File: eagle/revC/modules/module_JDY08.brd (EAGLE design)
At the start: 24.1 x 32.8 mm, 32 parts

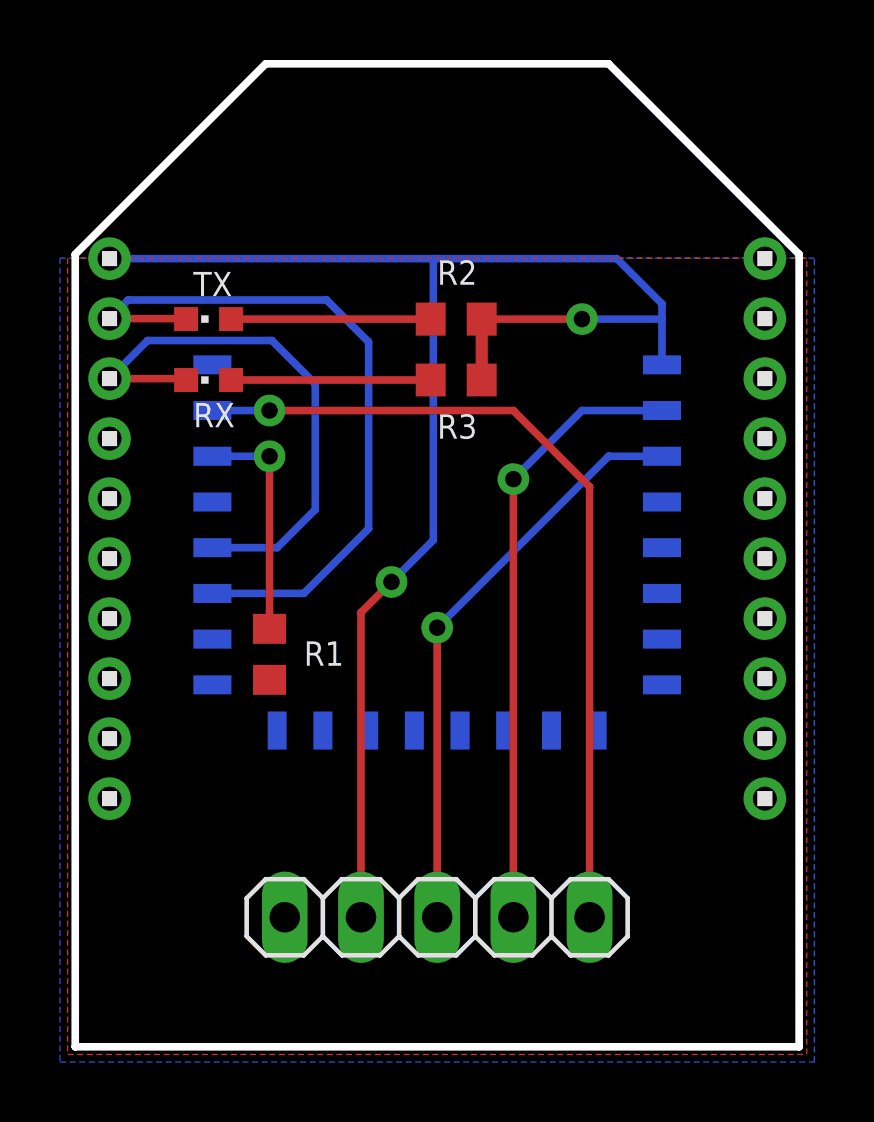
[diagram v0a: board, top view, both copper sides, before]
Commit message: Replaced modules with library parts
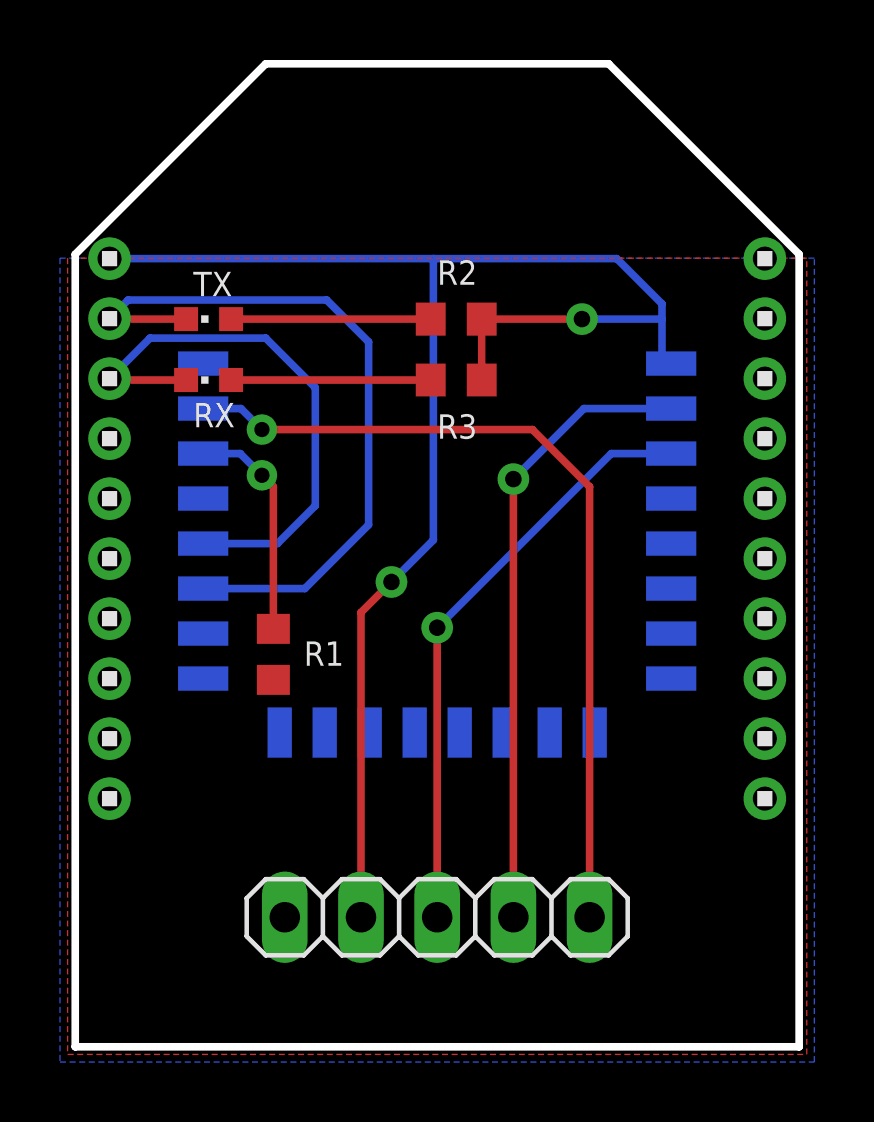
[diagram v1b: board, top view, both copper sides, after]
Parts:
- removed GND, P00, P01, P02, P03, P04, P05, P06, P07, P10, P11, P12, P13, P14, P15, P16, P17, P20, P21, P22, RST, SCL, SDA, VCC: (no value), wirepad:SMD0,65-1,27
- added U$1: JDY08, RadioShield:JDY08
- moved R1 0.13 mm to (6.73, 13.2), turned to 270 degrees
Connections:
- removed net N$5: LEFT1.3, P02.1, RX.C
- removed net N$6: LEFT1.2, P03.1, TX.C
- new net N$10: R1.1, U$1.P00
- new net N$11: LEFT1.2, TX.C, U$1.TXD
- net GND: now also R1.2, U$1.GND; no longer GND.1, R1.1
- net N$1: now also U$1.RST; no longer RST.1
- net N$2: now also U$1.P21; no longer P21.1
- net N$3: now also U$1.P22; no longer P22.1
- net N$4: now also LEFT1.3, RX.C, U$1.RXD; no longer P00.1, R1.2
- net VCC: now also U$1.VCC; no longer VCC.1
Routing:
- net N$11: track 0.00 -> 24.5 mm
- net N$6: track 24.4 -> 0.00 mm
- net N$5: track 18.7 -> 0.00 mm
- net N$4: track 7.66 -> 18.9 mm, vias 1 -> 0
- net N$10: track 0.00 -> 7.53 mm, vias 0 -> 1
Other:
- board text removed: "P00"
- board text removed: "P01"
- board text removed: "P02"
- board text removed: "P03"
- board text removed: "P04"
- board text removed: "P05"
- board text removed: "P06"
- board text removed: "P07"
- board text removed: "P10"
- board text removed: "P11"
- board text removed: "P12"
- board text removed: "P13"
- board text removed: "P14"
- board text removed: "P15"
- board text removed: "P16"
- board text removed: "P17"
- board text removed: "P20"
- board text removed: "P21"
- board text removed: "P22"
- board text removed: "SCL"
- board text removed: "SDA"

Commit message: Fixed module name layers
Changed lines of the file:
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@@
 <wire x1="24.257" y1="26.543" x2="24.257" y2="0.127" width="0.254" layer="20"/>
 <wire x1="24.257" y1="0.127" x2="0.127" y2="0.127" width="0.254" layer="20"/>
-<text x="16.383" y="1.778" size="0.8128" layer="51" font="vector" ratio="15" rot="SR0">RST</text>
-<text x="11.303" y="1.778" size="0.8128" layer="51" font="vector" ratio="15" rot="SR0">DAT</text>
-<text x="13.843" y="1.778" size="0.8128" layer="51" font="vector" ratio="15" rot="SR0">CLK</text>
-<text x="8.763" y="1.778" size="0.8128" layer="51" font="vector" ratio="15" rot="SR0">VCC</text>
-<text x="6.096" y="1.778" size="0.8128" layer="51" font="vector" ratio="15" rot="SR0">GND</text>
-<text x="18.161" y="1.778" size="0.8128" layer="52" font="vector" ratio="15" rot="SMR0">RST</text>
-<text x="13.081" y="1.778" size="0.8128" layer="52" font="vector" ratio="15" rot="SMR0">DAT</text>
-<text x="15.621" y="1.778" size="0.8128" layer="52" font="vector" ratio="15" rot="SMR0">CLK</text>
-<text x="10.541" y="1.778" size="0.8128" layer="52" font="vector" ratio="15" rot="SMR0">VCC</text>
-<text x="8.128" y="1.778" size="0.8128" layer="52" font="vector" ratio="15" rot="SMR0">GND</text>
-<text x="12.192" y="30.48" size="1.778" layer="51" ratio="15" rot="SR0" align="center">JDY-08</text>
+<text x="16.383" y="1.778" size="0.8128" layer="25" font="vector" ratio="15" rot="SR0">RST</text>
+<text x="11.303" y="1.778" size="0.8128" layer="25" font="vector" ratio="15" rot="SR0">DAT</text>
+<text x="13.843" y="1.778" size="0.8128" layer="25" font="vector" ratio="15" rot="SR0">CLK</text>
+<text x="8.763" y="1.778" size="0.8128" layer="25" font="vector" ratio="15" rot="SR0">VCC</text>
+<text x="6.096" y="1.778" size="0.8128" layer="25" font="vector" ratio="15" rot="SR0">GND</text>
+<text x="18.161" y="1.778" size="0.8128" layer="26" font="vector" ratio="15" rot="SMR0">RST</text>
+<text x="13.081" y="1.778" size="0.8128" layer="26" font="vector" ratio="15" rot="SMR0">DAT</text>
+<text x="15.621" y="1.778" size="0.8128" layer="26" font="vector" ratio="15" rot="SMR0">CLK</text>
+<text x="10.541" y="1.778" size="0.8128" layer="26" font="vector" ratio="15" rot="SMR0">VCC</text>
+<text x="8.128" y="1.778" size="0.8128" layer="26" font="vector" ratio="15" rot="SMR0">GND</text>
+<text x="12.192" y="30.48" size="1.778" layer="25" ratio="15" rot="SR0" align="center">JDY-08</text>
 <text x="7.747" y="12.827" size="0.8128" layer="125" font="vector" ratio="12" rot="SR0">R1</text>
 <text x="12.192" y="25.527" size="0.8128" layer="125" font="vector" ratio="12" rot="SR0">R2</text>
